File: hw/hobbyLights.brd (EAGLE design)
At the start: 50 x 35.1 mm, 56 parts, among them U1 MCP73831-2, U2 POWER, U3 BD48K28G, U4 ATMEGA32U4-AU, U5 TPS61222, Y1 RESONATORSMD

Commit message: Minor updates.
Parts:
- C13: device rcl:C0603 -> fmc:C0603
- moved C9 0.38 mm to (29.7, 3.30)
- moved C17 0.25 mm to (29.7, 1.52)
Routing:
- net N$15: track 7.03 -> 5.14 mm
- net GND: vias 93 -> 97
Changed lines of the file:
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@@
 </element>
 <element name="R11" library="fmc" package="R0603" value="10k" x="22.098" y="19.05" smashed="yes" rot="R90">
-<attribute name="NAME" x="23.241" y="21.463" size="0.8128" layer="25" ratio="12" rot="R180"/>
+<attribute name="NAME" x="23.368" y="21.717" size="0.8128" layer="25" ratio="12" rot="R180"/>
 <attribute name="VALUE" x="24.003" y="17.145" size="0.8128" layer="27" ratio="12" rot="R90"/>
 </element>
@@
 <attribute name="VALUE" x="34.671" y="10.287" size="0.8128" layer="27" ratio="12" rot="R270"/>
 </element>
-<element name="C9" library="fmc" package="C0603" value="0.1uF" x="29.718" y="3.683" smashed="yes">
-<attribute name="NAME" x="33.02" y="4.318" size="0.8128" layer="25" ratio="12" rot="R180"/>
-<attribute name="VALUE" x="27.432" y="1.651" size="0.8128" layer="27" ratio="12"/>
+<element name="C9" library="fmc" package="C0603" value="0.1uF" x="29.718" y="3.302" smashed="yes">
+<attribute name="NAME" x="33.02" y="3.937" size="0.8128" layer="25" ratio="12" rot="R180"/>
+<attribute name="VALUE" x="27.432" y="1.27" size="0.8128" layer="27" ratio="12"/>
 </element>
 <element name="C10" library="fmc" package="C0603" value="0.1uF" x="19.431" y="11.303" smashed="yes" rot="R90">
@@
 <element name="U$6" library="fmc" package="BOARD_REF" value="" x="43.18" y="6.35" rot="MR0"/>
 <element name="U$7" library="fmc" package="GEEKKIDS_S" value="" x="43.18" y="24.003" rot="MR0"/>
-<element name="C13" library="rcl" package="C0603" value="0.1uF" x="34.163" y="18.796" smashed="yes" rot="R270">
+<element name="C13" library="fmc" package="C0603" value="0.1uF" x="34.163" y="18.796" smashed="yes" rot="R270">
 <attribute name="NAME" x="35.052" y="19.304" size="0.8128" layer="25" font="vector" ratio="12"/>
 <attribute name="VALUE" x="32.258" y="19.431" size="1.27" layer="27" rot="R270"/>
@@
 <attribute name="VALUE" x="-0.014" y="29.548" size="1.27" layer="27" rot="R270"/>
 </element>
-<element name="C17" library="fmc" package="C0603" value="1uF" x="29.718" y="1.778" smashed="yes">
-<attribute name="NAME" x="31.623" y="1.27" size="0.8128" layer="25" ratio="12"/>
-<attribute name="VALUE" x="27.432" y="-0.254" size="0.8128" layer="27" ratio="12"/>
+<element name="C17" library="fmc" package="C0603" value="1uF" x="29.718" y="1.524" smashed="yes">
+<attribute name="NAME" x="31.623" y="1.016" size="0.8128" layer="25" ratio="12"/>
+<attribute name="VALUE" x="27.432" y="-0.508" size="0.8128" layer="27" ratio="12"/>
 </element>
 <element name="TM1" library="adafruit" package="TC33X" value="" x="40.132" y="28.448" smashed="yes" rot="R270">
@@
 <contactref element="U$4" pad="GND"/>
 <via x="31.877" y="2.413" extent="1-16" drill="0.3"/>
-<via x="31.877" y="3.302" extent="1-16" drill="0.3"/>
+<via x="31.877" y="3.683" extent="1-16" drill="0.3"/>
 <contactref element="C13" pad="2"/>
 <contactref element="C14" pad="2"/>
@@
 <via x="14.351" y="30.099" extent="1-16" drill="0.3"/>
 <via x="15.621" y="23.749" extent="1-16" drill="0.3"/>
-<via x="18.669" y="21.59" extent="1-16" drill="0.3"/>
+<via x="17.78" y="20.32" extent="1-16" drill="0.3"/>
 <via x="12.065" y="23.368" extent="1-16" drill="0.3"/>
-<via x="15.494" y="18.542" extent="1-16" drill="0.3"/>
-<via x="15.494" y="17.526" extent="1-16" drill="0.3"/>
 <via x="13.208" y="18.161" extent="1-16" drill="0.3"/>
 <via x="11.557" y="15.113" extent="1-16" drill="0.3"/>
@@
 <via x="4.826" y="21.59" extent="1-16" drill="0.3"/>
 <via x="6.35" y="28.575" extent="1-16" drill="0.3"/>
+<via x="17.78" y="17.78" extent="1-16" drill="0.3"/>
+<via x="16.51" y="17.78" extent="1-16" drill="0.3"/>
+<via x="17.78" y="22.86" extent="1-16" drill="0.3"/>
+<via x="36.957" y="30.226" extent="1-16" drill="0.3"/>
+<via x="36.957" y="28.702" extent="1-16" drill="0.3"/>
+<via x="17.78" y="25.4" extent="1-16" drill="0.3"/>
 </signal>
 <signal name="N$4">
@@
 <wire x1="28.867" y1="8.103" x2="28.867" y2="8.039" width="0.254" layer="1"/>
 <wire x1="28.867" y1="8.039" x2="28.7655" y2="7.9375" width="0.254" layer="1"/>
-<wire x1="28.868" y1="3.683" x2="28.868" y2="6.391" width="0.3048" layer="1"/>
+<wire x1="28.868" y1="3.302" x2="28.868" y2="6.391" width="0.3048" layer="1"/>
 <wire x1="28.868" y1="6.391" x2="28.867" y2="6.392" width="0.3048" layer="1"/>
 <wire x1="12.108" y1="16.637" x2="12.954" y2="16.637" width="0.254" layer="1"/>
@@
 <wire x1="19.431" y1="16.192" x2="18.351" y2="16.192" width="0.3048" layer="1"/>
 <wire x1="18.351" y1="16.192" x2="18.161" y2="16.002" width="0.3048" layer="1"/>
-<wire x1="18.161" y1="16.002" x2="16.256" y2="16.002" width="0.3048" layer="1"/>
-<wire x1="16.256" y1="16.002" x2="16.129" y2="16.002" width="0.3048" layer="1"/>
+<wire x1="18.161" y1="16.002" x2="16.129" y2="16.002" width="0.3048" layer="1"/>
 <wire x1="15.748" y1="16.002" x2="16.129" y2="16.002" width="0.3048" layer="1"/>
 </signal>
@@
 <wire x1="19.05" y1="29.591" x2="23.622" y2="29.591" width="0.4064" layer="1"/>
 <wire x1="23.622" y1="29.591" x2="24.13" y2="29.591" width="0.4064" layer="1"/>
-<wire x1="26.467" y1="17.992" x2="26.467" y2="19.253" width="0.3048" layer="1"/>
-<wire x1="26.467" y1="19.253" x2="26.289" y2="19.431" width="0.3048" layer="1"/>
-<via x="26.289" y="19.431" extent="1-16" drill="0.35"/>
-<wire x1="26.289" y1="19.431" x2="26.289" y2="24.511" width="0.3048" layer="16"/>
-<wire x1="26.289" y1="24.511" x2="22.86" y2="28.067" width="0.3048" layer="16"/>
+<wire x1="26.467" y1="17.992" x2="26.467" y2="20.396" width="0.3048" layer="1"/>
+<wire x1="26.467" y1="20.396" x2="26.162" y2="20.701" width="0.3048" layer="1"/>
+<via x="26.162" y="20.701" extent="1-16" drill="0.35"/>
+<wire x1="26.162" y1="20.701" x2="26.162" y2="24.638" width="0.3048" layer="16"/>
+<wire x1="26.162" y1="24.638" x2="22.86" y2="28.067" width="0.3048" layer="16"/>
 <via x="22.86" y="28.067" extent="1-16" drill="0.35"/>
 <wire x1="22.86" y1="28.067" x2="22.86" y2="28.829" width="0.3048" layer="1"/>
@@
 <contactref element="S2" pad="4"/>
 <wire x1="27.432" y1="29.591" x2="32.512" y2="29.591" width="0.4064" layer="1"/>
-<wire x1="27.267" y1="17.992" x2="27.267" y2="20.104" width="0.3048" layer="1"/>
-<wire x1="27.267" y1="20.104" x2="27.178" y2="20.193" width="0.3048" layer="1"/>
-<via x="27.178" y="20.193" extent="1-16" drill="0.35"/>
-<wire x1="27.178" y1="20.193" x2="27.178" y2="26.289" width="0.3048" layer="16"/>
-<wire x1="27.178" y1="26.289" x2="25.781" y2="27.686" width="0.3048" layer="16"/>
+<wire x1="27.267" y1="17.992" x2="27.267" y2="20.739" width="0.3048" layer="1"/>
+<wire x1="27.267" y1="20.739" x2="27.559" y2="21.082" width="0.3048" layer="1"/>
+<via x="27.559" y="21.082" extent="1-16" drill="0.35"/>
+<wire x1="27.559" y1="21.082" x2="27.559" y2="25.908" width="0.3048" layer="16"/>
+<wire x1="27.559" y1="25.908" x2="25.781" y2="27.686" width="0.3048" layer="16"/>
 <wire x1="25.781" y1="27.686" x2="25.781" y2="28.067" width="0.3048" layer="16"/>
 <via x="25.781" y="28.067" extent="1-16" drill="0.35"/>
@@
 <wire x1="28.067" y1="6.392" x2="28.067" y2="5.207" width="0.254" layer="1"/>
 <wire x1="28.067" y1="5.207" x2="27.813" y2="4.953" width="0.254" layer="1"/>
-<wire x1="27.813" y1="4.953" x2="27.813" y2="2.032" width="0.254" layer="1"/>
-<wire x1="27.813" y1="2.032" x2="28.067" y2="1.778" width="0.254" layer="1"/>
-<wire x1="28.067" y1="1.778" x2="28.868" y2="1.778" width="0.254" layer="1"/>
+<wire x1="27.813" y1="4.953" x2="27.813" y2="1.778" width="0.254" layer="1"/>
+<wire x1="27.813" y1="1.778" x2="28.067" y2="1.524" width="0.254" layer="1"/>
+<wire x1="28.067" y1="1.524" x2="28.868" y2="1.524" width="0.254" layer="1"/>
 </signal>
 <signal name="N$13">
@@
 <contactref element="U5" pad="5"/>
 <contactref element="L1" pad="2"/>
-<wire x1="14.308" y1="16.637" x2="16.383" y2="16.637" width="0.3556" layer="1"/>
-<wire x1="16.383" y1="16.637" x2="16.637" y2="16.891" width="0.3556" layer="1"/>
-<wire x1="16.637" y1="16.891" x2="16.637" y2="19.304" width="0.3556" layer="1"/>
-<wire x1="16.637" y1="19.304" x2="16.002" y2="19.939" width="0.3556" layer="1"/>
-<wire x1="16.002" y1="19.939" x2="16.002" y2="20.296" width="0.3556" layer="1"/>
-<wire x1="16.002" y1="20.296" x2="15.343" y2="20.955" width="0.3556" layer="1"/>
+<wire x1="15.343" y1="20.955" x2="15.343" y2="16.994" width="0.3048" layer="1"/>
+<wire x1="15.343" y1="16.994" x2="14.986" y2="16.637" width="0.3048" layer="1"/>
+<wire x1="14.986" y1="16.637" x2="14.308" y2="16.637" width="0.3048" layer="1"/>
 </signal>
 <signal name="N$16">

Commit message: Made adjustments to the board.
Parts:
- removed U$10, U$6: (no value), fmc:BOARD_REF
- added U$23: (no value), fmc:USB_LOGO
- added U$24: (no value), fmc:BOARD_REF_M
- C8: device rcl:C0603 -> fmc:C0603
- moved U$11 22.0 mm to (40.6, 0.38)
- moved U$7 20.2 mm to (30.7, 8.13)
- moved U$5 12.8 mm to (27.8, 0.38)
- moved U$17 0.64 mm to (35.7, 30.9)
- moved CN1 0.46 mm to (2.79, 22.2)
- moved C10 0.25 mm to (19.4, 11.0)
- moved R11 0.25 mm to (22.1, 18.8)
- moved C3 0.13 mm to (19.4, 1.91)
- moved R3 0.13 mm to (19.4, 3.94)
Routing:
- net D10: track 24.1 -> 24.7 mm
- net A0: track 39.0 -> 39.6 mm
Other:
- board text added: "By: F. Malpartida"
- board text removed: "USB"

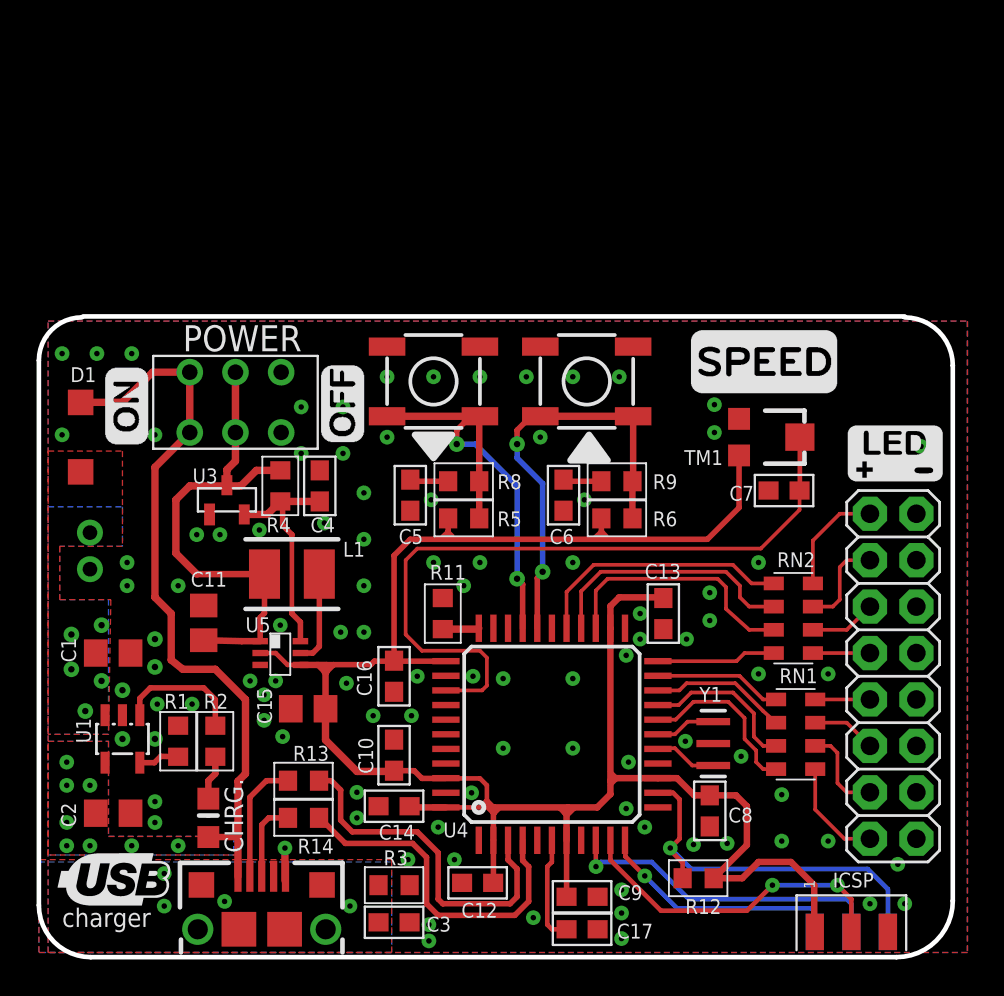
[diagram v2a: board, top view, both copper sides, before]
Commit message: Added motor support.
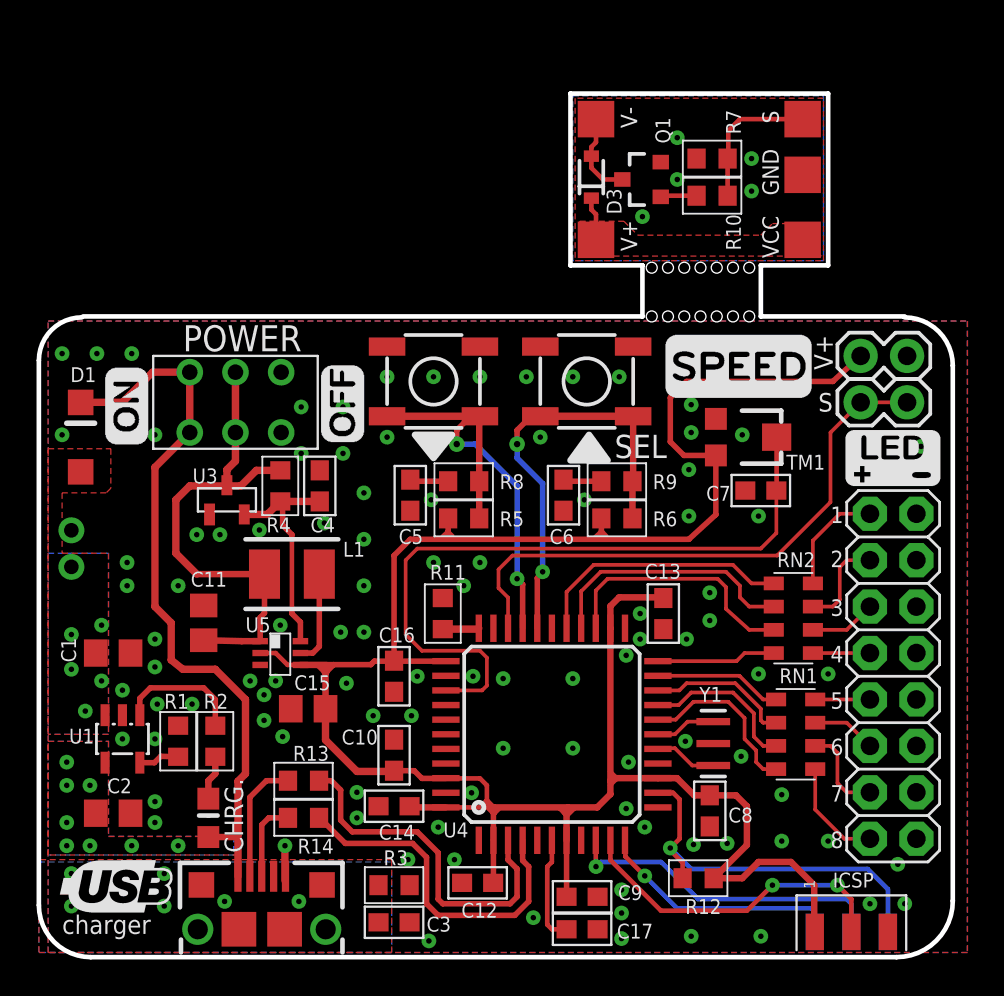
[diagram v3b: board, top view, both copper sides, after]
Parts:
- added D3: BAT20J, SparkFun-DiscreteSemi:SOD-323
- added GND, S, V+, V-, VCC: TPTP20SQ, testpad:TP20SQ
- added J2, J3: (no value), SparkFun-Connectors:1X02
- added Q1: PMV22EN, SparkFun-DiscreteSemi:SOT23-3
- added R10: 22R, fmc:R0603
- added R7: 10k, fmc:R0603
- moved U$17 1.42 mm to (34.3, 30.6)
- moved C7 1.27 mm to (39.5, 25.5)
- moved TM1 1.27 mm to (38.9, 28.4)
- moved CN1 1.02 mm to (1.78, 22.4), turned to 270 degrees
- moved U$23 0.40 mm to (1.14, 1.02)
- moved U$1 0.28 mm to (44.1, 25.8)
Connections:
- new net GND1: GND.TP, Q1.2, R7.2
- new net N$1: Q1.1, R10.2
- new net N$10: D3.A, Q1.3, V-.TP
- new net N$8: R10.1, R7.1, S.TP
- new net V+: D3.C, V+.TP, VCC.TP
- net D5: now also J3.1, J3.2
- net GND: now also J2.2
- net VCC: now also J2.1
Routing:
- net D5: track 0.00 -> 31.8 mm
- net VCC: track 119.7 -> 135.2 mm
- net N$8: track 0.00 -> 7.90 mm
- net N$10: track 0.00 -> 4.73 mm
- net V+: track 0.00 -> 2.38 mm
- net N$1: track 0.00 -> 1.99 mm
- net A0: track 39.6 -> 39.1 mm
- net GND: track 2.00 -> 2.12 mm, vias 97 -> 100
- added copper zone on layer 1, net GND1
- added copper zone on layer 16, net GND1
- added copper zone on layer 1, net V+
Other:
- board size 50 x 35.1 mm -> 50 x 47.2 mm
- board text added: "1"
- board text added: "2"
- board text added: "3"
- board text added: "4"
- board text added: "5"
- board text added: "6"
- board text added: "7"
- board text added: "8"
- board text added: "Motor Cntrl"
- board text added: "Rev A."
- board text added: "S"
- board text added: "SEL"
- board text added: "V+"
- board text added: "electroFUN LTD"

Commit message: Minor updates and silk screen improvements.
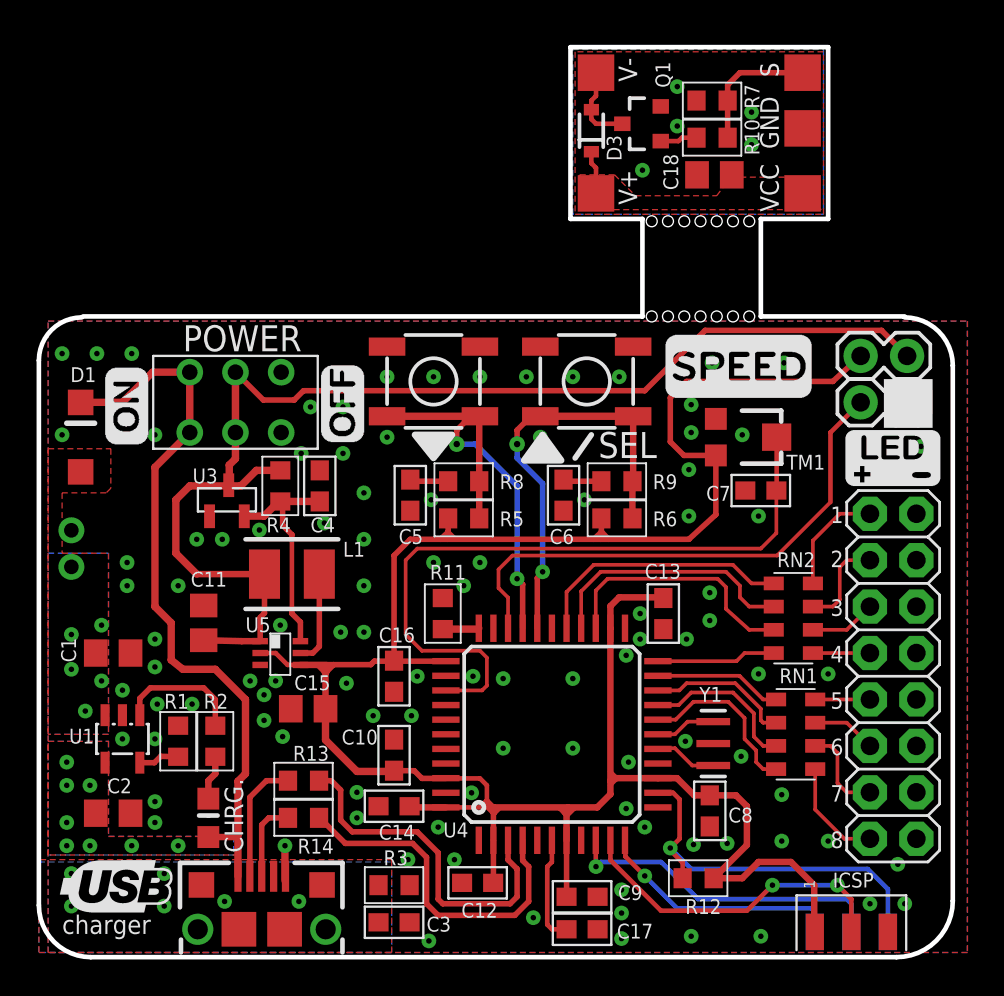
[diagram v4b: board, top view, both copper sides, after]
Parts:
- added C18: 10uF, rcl:C0805
- moved U$24 5.91 mm to (43.3, 14.0)
- moved U$5 3.81 mm to (31.6, 0.38)
- moved U$7 3.81 mm to (34.5, 8.13)
- moved R10 3.18 mm to (36.8, 44.8)
- moved R7 3.17 mm to (36.8, 46.9)
- moved Q1 3.05 mm to (33.0, 45.6)
- moved D3 2.54 mm to (30.2, 45.2)
- moved GND 2.54 mm to (41.8, 45.3)
- moved S 2.54 mm to (41.8, 48.4)
- moved V+ 2.54 mm to (30.5, 41.8)
- moved V- 2.54 mm to (30.5, 48.4)
- moved VCC 2.54 mm to (41.8, 41.8)
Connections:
- net D5: no longer J3.2
- net GND: now also J3.2; no longer J2.2
- net GND1: now also C18.2
- net V+: now also C18.1
- net V_BATT: now also J2.2
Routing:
- net V_BATT: track 27.9 -> 67.3 mm
- net D5: track 31.8 -> 29.3 mm
- net N$8: track 7.90 -> 7.26 mm
- net GND: vias 100 -> 102
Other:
- board size 50 x 47.2 mm -> 50 x 49.8 mm
- board text added: "5V"
- board text added: "GND"
- board text added: "Vb"
- board text removed: "V+"
